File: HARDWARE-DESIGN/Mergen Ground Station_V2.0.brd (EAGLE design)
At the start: 72.4 x 94.9 mm, 68 parts, among them J1 USB_A_SMT_FEMALE_NS, J2 CON-SD-CARD_MICROSD-2908-05, J4 U.FL, U1 STM32F302C8T6, U13 L86, U15 AMS1117-5V, U16 AMS1117-3.3, X2 JST-XH-04-PIN-LONG-PAD, Y1 ABMM2-8.000MHZ-E2-T

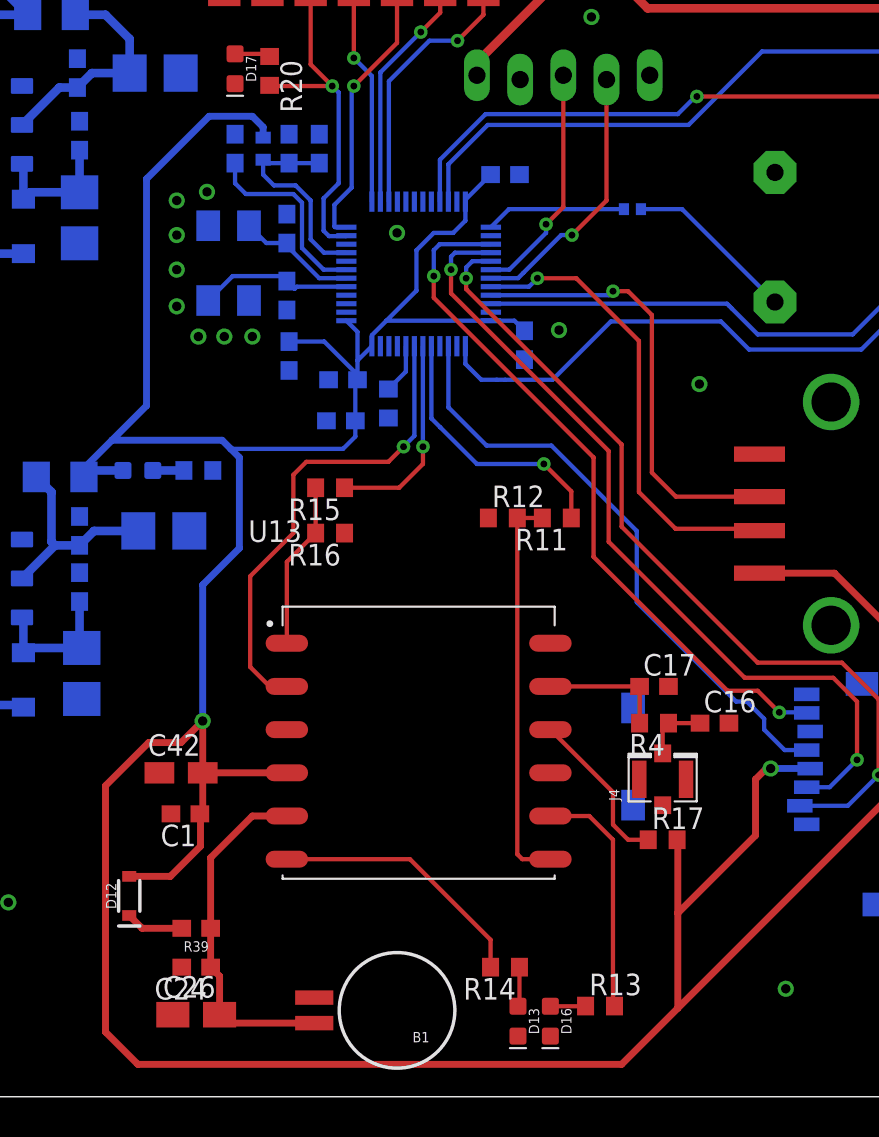
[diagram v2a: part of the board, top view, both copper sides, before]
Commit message: packages was modified according to stock situation
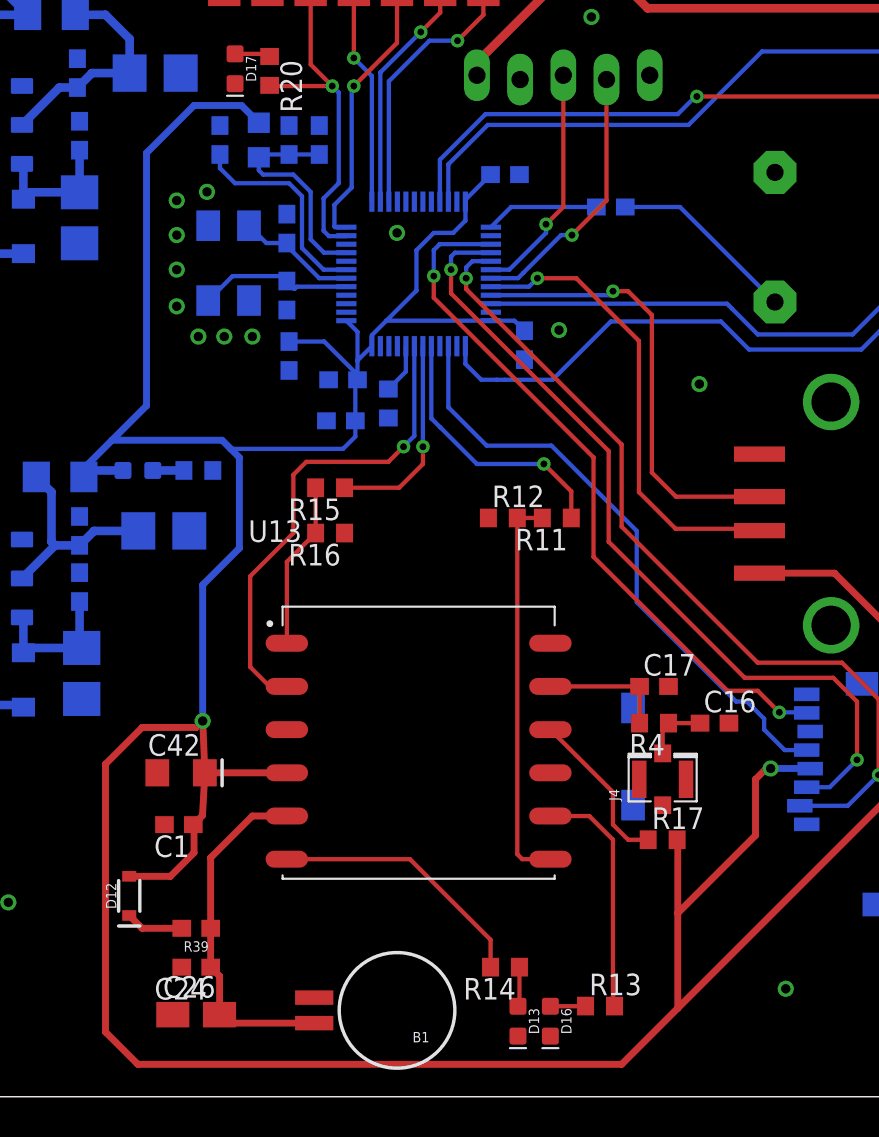
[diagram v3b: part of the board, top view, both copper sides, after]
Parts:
- C42: device rcl:R/2012-12W -> SparkFun-Capacitors:EIA3216
- L2: value BLM15HB221SN1 -> (none); device inductors:0402 -> 52101-101-REV-A_v16:RC-MASTER-SMD_L0805MP
- R32: device rcl:R0402 -> SparkFun-Resistors:0603
- moved R32 1.28 mm to (46.9, 57.4)
- moved C23 1.02 mm to (23.9, 61.3)
- moved C1 0.74 mm to (21.5, 21.1)
- moved L2 0.57 mm to (26.2, 61.3)
- moved VDDA3 0.51 mm to (27.9, 61.3)
- moved VDDA4 0.51 mm to (29.7, 61.3)
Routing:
- net BZZR: track 8.26 -> 6.69 mm
- net NRST: track 11.4 -> 12.5 mm
- net 3.3V: track 263.8 -> 264.9 mm
- net N$28: track 10.1 -> 11.1 mm
- net VDDA: track 12.4 -> 13.2 mm
